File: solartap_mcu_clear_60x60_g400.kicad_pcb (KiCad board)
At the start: 2 copper layers, 70 x 70 mm, 24 parts, among them J1 USB_C_Receptacle_USB2.0_16P, U1 nRF52832-QFxx, U2 RS3002-3.3SYF5

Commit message: Продовая версия без fiducials
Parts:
- removed C13: 100n, Capacitor_SMD:C_0805_2012Metric_Pad1.18x1.45mm_HandSolder
- removed TP6: GND, TestPoint:TestPoint_Pad_D2.0mm
- added C7: 100p, Capacitor_SMD:C_0805_2012Metric, F.Cu at (86.5, 69.0)
- added C8: 100n, Capacitor_SMD:C_0805_2012Metric, F.Cu at (90.5, 57.0)
- added C9: TBD, Capacitor_SMD:C_0805_2012Metric, F.Cu at (86.0, 57.0)
- added TP4: GND, TestPoint:TestPoint_Pad_D2.0mm, F.Cu at (62.0, 64.5)
- added Y1: 32Mhz, Crystal:Crystal_SMD_3225-4Pin_3.2x2.5mm, F.Cu at (94.0, 69.5)
- BT1: value CR2032 -> CR927; footprint Battery:BatteryHolder_MPD_BC2003_1x2032 -> Battery:CR927
- C1: value 100n -> 16p; footprint Capacitor_SMD:C_0805_2012Metric_Pad1.18x1.45mm_HandSolder -> Capacitor_SMD:C_0805_2012Metric
- C10, C12: footprint Capacitor_SMD:C_0805_2012Metric_Pad1.18x1.45mm_HandSolder -> Capacitor_SMD:C_0805_2012Metric
- C11: value TBD -> 100n; footprint Capacitor_SMD:C_0805_2012Metric_Pad1.18x1.45mm_HandSolder -> Capacitor_SMD:C_0805_2012Metric
- C2: value 100p -> 16p; footprint Capacitor_SMD:C_0805_2012Metric_Pad1.18x1.45mm_HandSolder -> Capacitor_SMD:C_0805_2012Metric
- C3: value 1u -> 100n; footprint Capacitor_SMD:C_0805_2012Metric_Pad1.18x1.45mm_HandSolder -> Capacitor_SMD:C_0805_2012Metric
- C4: value 100n -> 4.7u; footprint Capacitor_SMD:C_0805_2012Metric_Pad1.18x1.45mm_HandSolder -> Capacitor_SMD:C_0805_2012Metric
- C5: value 4.7u -> 100n; footprint Capacitor_SMD:C_0805_2012Metric_Pad1.18x1.45mm_HandSolder -> Capacitor_SMD:C_0805_2012Metric
- C6: value 100n -> 1u; footprint Capacitor_SMD:C_0805_2012Metric_Pad1.18x1.45mm_HandSolder -> Capacitor_SMD:C_0805_2012Metric
- D1: moved to B.Cu
- D2: value RB751S-40 -> LBAT54CLT1G; footprint Diode_SMD:D_SOD-523 -> Package_TO_SOT_SMD:SOT-23-3
- J1: footprint Connector_USB:USB_C_Receptacle_GCT_USB4110 -> Connector_USB:USB_C_Receptacle_GCT_USB4105-xx-A_16P_TopMnt_Horizontal
- R1: value 100 -> 75; footprint Resistor_SMD:R_0805_2012Metric_Pad1.20x1.40mm_HandSolder -> Resistor_SMD:R_0805_2012Metric
- R2, R3: footprint Resistor_SMD:R_0805_2012Metric_Pad1.20x1.40mm_HandSolder -> Resistor_SMD:R_0805_2012Metric
- TP1: value RESET -> IO
- TP3: value IO -> RESET
- U2: footprint Package_TO_SOT_SMD:SOT-23-3 -> Package_TO_SOT_SMD:SOT-23-5
- moved TP5 72.7 mm to (62.0, 68.0)
- moved C11 56.6 mm to (112.5, 107.0), turned to -90 degrees
- moved R1 32.2 mm to (80.5, 75.0), turned to -90 degrees
- moved C5 14.2 mm to (80.0, 60.5)
- moved C4 13.7 mm to (94.0, 58.0)
- moved C1 12.5 mm to (90.5, 69.5), turned to 90 degrees
- moved C2 11.0 mm to (97.5, 69.5), turned to -90 degrees
- moved D1 11.0 mm to (70.0, 106.9)
- moved TP3 9.00 mm to (62.0, 71.5)
- moved TP1 7.00 mm to (62.0, 78.5)
- moved C3 3.20 mm to (91.5, 64.0), turned to 90 degrees
- moved C6 3.20 mm to (94.0, 62.0), turned to -90 degrees
- moved D2 3.16 mm to (115.5, 107.0), turned to 90 degrees
- moved TP2 1.00 mm to (62.0, 75.0)
- moved J1 0.50 mm to (95.0, 107.5)
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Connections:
- BT1 pad 1: +3.3V -> Net-(BT1-+)
- C1 pad 1: Net-(U1-DEC1) -> Net-(U1-XC1)
- C10 pad 1: GND -> Net-(U1-NFC1/P0.09)
- C10 pad 2: Net-(U1-NFC1/P0.09) -> GND
- C11 pad 1: Net-(U1-NFC1/P0.09) -> Net-(U2-OUT)
- C12 pad 1: Net-(U2-IN) -> Net-(U2-EN)
- C2 pad 1: Net-(U1-DEC3) -> Net-(U1-XC2)
- C3 pad 1: Net-(U1-DEC4) -> +3.3V
- C6 pad 1: +3.3V -> Net-(U1-DEC4)
- D1 pad 2: Net-(D1-A) -> +3.3V
- D2 pad 1: +3.3V -> Net-(U2-OUT)
- D2 pad 2: Net-(D2-A) -> Net-(BT1-+)
- J1 pad A4: Net-(U2-IN) -> Net-(U2-EN)
- J1 pad A9: Net-(U2-IN) -> Net-(U2-EN)
- J1 pad B4: Net-(U2-IN) -> Net-(U2-EN)
- J1 pad B9: Net-(U2-IN) -> Net-(U2-EN)
- R1 pad 1: Net-(D1-A) -> Net-(U1-P0.22)
- R1 pad 2: +3.3V -> Net-(D1-K)
- TP1 pad 1: Net-(U1-P0.21/~{RESET}) -> Net-(U1-SWDIO)
- TP3 pad 1: Net-(U1-SWDIO) -> Net-(U1-P0.21/~{RESET})
- U1 pad 27: Net-(D1-K) -> Net-(U1-P0.22)
- U1 pad 28: unconnected-(U1-P0.23-Pad28) -> Net-(D1-K)
- U1 pad 34: unconnected-(U1-XC1-Pad34) -> Net-(U1-XC1)
- U1 pad 35: unconnected-(U1-XC2-Pad35) -> Net-(U1-XC2)
- U2 pad 1: GND -> Net-(U2-EN)
- U2 pad 2: Net-(D2-A) -> GND
- U2 pad 3: Net-(U2-IN) -> Net-(U2-EN)
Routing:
- net Net-(BT1-+): track 0.00 -> 37.0 mm
- net GND: track 119.1 -> 154.5 mm, vias 9 -> 8
- net Net-(U2-EN): track 0.00 -> 23.1 mm
- net Net-(U2-IN): track 21.4 -> 0.00 mm
- net Net-(U1-XC2): track 0.00 -> 10.7 mm
- net Net-(U1-P0.22): track 0.00 -> 10.0 mm
- net Net-(U1-XC1): track 0.00 -> 8.14 mm
- net Net-(D2-A): track 5.95 -> 0.00 mm
- net unconnected-(U1-P0.24-Pad29): track 0.00 -> 5.84 mm
- net unconnected-(U1-P0.20-Pad23): track 0.00 -> 5.46 mm
- net Net-(U2-OUT): track 0.00 -> 5.42 mm
- net Net-(D1-K): track 41.8 -> 47.1 mm, vias 0 -> 1
- net unconnected-(U1-P0.19-Pad22): track 0.00 -> 5.21 mm
- net unconnected-(U1-P0.18/SWO-Pad21): track 0.00 -> 4.96 mm
- net unconnected-(U1-P0.17-Pad20): track 0.00 -> 4.72 mm
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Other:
- outline, holes or cut-outs redrawn
- board text added: "+"
- board text added: "+ БАТАРЕЙКИ ВВЕРХ"
- board text added: "20"
- board text added: "21"
- board text added: "22"
- board text added: "23"
- board text added: "29"
- board text added: "CR927 3V"
- board text added: "SolarTap/rev.D"
- board text removed: "G=400/C=15.249"

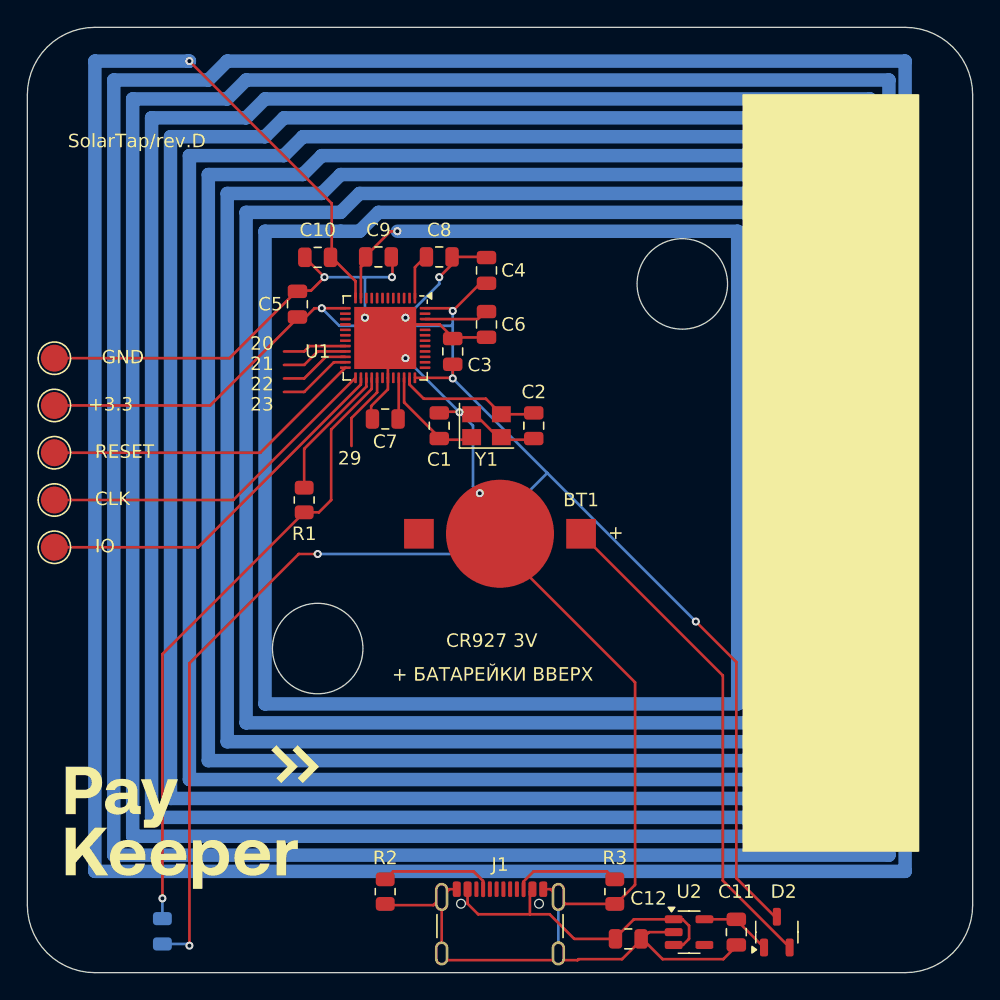
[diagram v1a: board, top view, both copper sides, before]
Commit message: Добавили fiducials
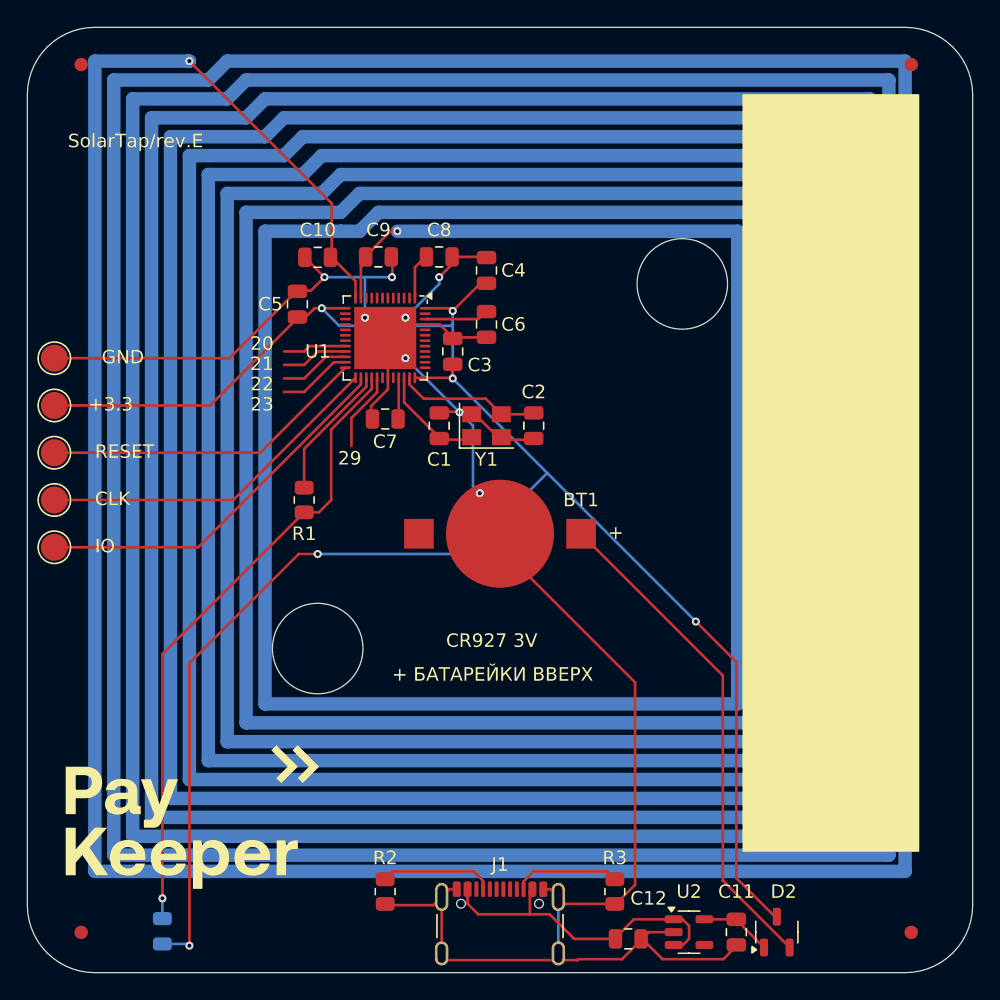
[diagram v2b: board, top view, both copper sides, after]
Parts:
- added REF**: Fiducial_1mm_Mask3mm, Fiducial:Fiducial_1mm_Mask3mm, F.Cu at (64.0, 107.0)
- added REF**: Fiducial_1mm_Mask3mm, Fiducial:Fiducial_1mm_Mask3mm, F.Cu at (125.5, 42.8)
- added REF**: Fiducial_1mm_Mask3mm, Fiducial:Fiducial_1mm_Mask3mm, F.Cu at (125.5, 107.0)
- added REF**: Fiducial_1mm_Mask3mm, Fiducial:Fiducial_1mm_Mask3mm, F.Cu at (64.0, 42.8)
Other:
- board text added: "SolarTap/rev.E"
- board text removed: "SolarTap/rev.D"

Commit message: Переделали схему под аккомулятор + добавили его чарджер. rev.F
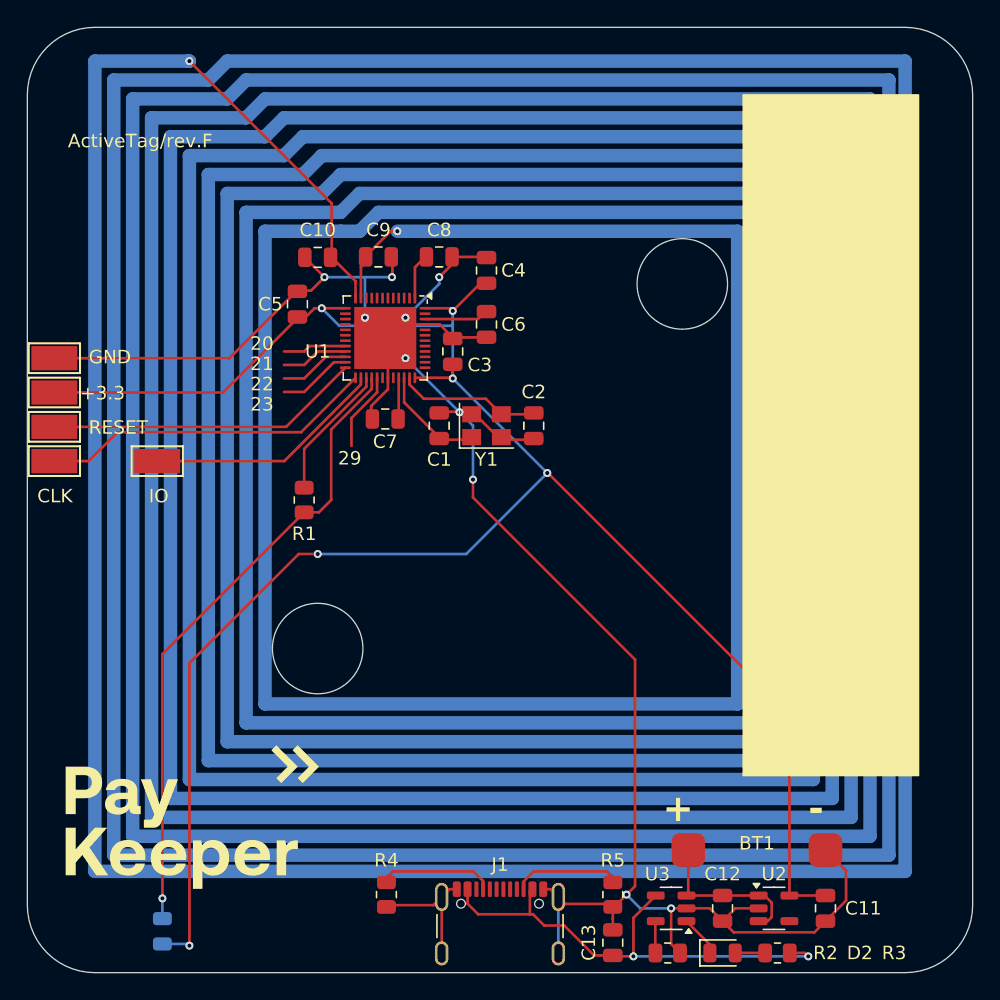
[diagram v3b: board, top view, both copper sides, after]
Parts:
- removed REF** (x4): Fiducial_1mm_Mask3mm, Fiducial:Fiducial_1mm_Mask3mm
- added C13: 100n, Capacitor_SMD:C_0805_2012Metric, F.Cu at (103.4, 107.8)
- added R4: 5.1k, Resistor_SMD:R_0805_2012Metric, F.Cu at (86.6, 104.2)
- added R5: 5.1k, Resistor_SMD:R_0805_2012Metric, F.Cu at (103.4, 104.2)
- added U3: LTC4054ES5-4.2, Package_TO_SOT_SMD:TSOT-23-5, F.Cu at (107.7, 105.2)
- BT1: value CR927 -> Li-Pol; footprint Battery:CR927 -> Battery:li-pol
- D2: value LBAT54CLT1G -> CHARGE; footprint Package_TO_SOT_SMD:SOT-23-3 -> LED_SMD:LED_0805_2012Metric
- R2: value 5.1k -> 10k
- TP1, TP2, TP3, TP4, TP5: footprint TestPoint:TestPoint_Pad_D2.0mm -> TestPoint:TestPoint_Keystone_5015_Micro-Minature
- moved BT1 30.2 mm to (114.0, 100.9)
- moved R2 21.4 mm to (107.4, 108.5), turned to 0 degrees
- moved R3 12.9 mm to (115.5, 108.5), turned to 180 degrees
- moved TP1 9.94 mm to (69.6, 72.1)
- moved C12 7.34 mm to (111.5, 105.2), turned to -90 degrees
- moved C11 6.83 mm to (119.1, 105.2)
- moved U2 6.53 mm to (115.3, 105.2)
- moved D2 4.30 mm to (111.5, 108.5), turned to 0 degrees
- moved TP2 2.88 mm to (62.0, 72.1)
- moved TP3 1.92 mm to (62.0, 69.6)
- moved TP5 0.96 mm to (62.0, 67.0)
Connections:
- C11 pad 1: Net-(U2-OUT) -> +3.3V
- C12 pad 1: Net-(U2-EN) -> Net-(BT1-+)
- D2 pad 1: Net-(U2-OUT) -> Net-(D2-K)
- D2 pad 2: Net-(BT1-+) -> Net-(D2-A)
- J1 pad A4: Net-(U2-EN) -> Net-(U3-V_{CC})
- J1 pad A9: Net-(U2-EN) -> Net-(U3-V_{CC})
- J1 pad B4: Net-(U2-EN) -> Net-(U3-V_{CC})
- J1 pad B9: Net-(U2-EN) -> Net-(U3-V_{CC})
- R2 pad 1: GND -> Net-(U3-PROG)
- R2 pad 2: Net-(J1-CC1) -> GND
- R3 pad 1: Net-(J1-CC2) -> Net-(U3-V_{CC})
- R3 pad 2: GND -> Net-(D2-A)
- U2 pad 1: Net-(U2-EN) -> Net-(BT1-+)
- U2 pad 3: Net-(U2-EN) -> Net-(BT1-+)
- U2 pad 5: Net-(U2-OUT) -> +3.3V
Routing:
- net Net-(U3-V_{CC}): track 0.00 -> 36.0 mm, vias 0 -> 2
- net Net-(BT1-+): track 37.0 -> 12.1 mm
- net Net-(U2-EN): track 23.1 -> 0.00 mm
- net Net-(U1-SWDIO): track 28.2 -> 17.9 mm
- net GND: track 154.5 -> 164.2 mm, vias 8 -> 10
- net Net-(U2-OUT): track 5.42 -> 0.00 mm
- net Net-(D2-K): track 0.00 -> 3.07 mm
- net Net-(U3-PROG): track 0.00 -> 2.36 mm
- net Net-(D2-A): track 0.00 -> 2.21 mm
- net +3.3V: track 153.8 -> 154.8 mm
- net Net-(U1-P0.21/~{RESET}): track 24.2 -> 23.4 mm
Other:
- board text added: "ActiveTag/rev.F"
- board text removed: "+"
- board text removed: "+ БАТАРЕЙКИ ВВЕРХ"
- board text removed: "CR927 3V"
- board text removed: "SolarTap/rev.E"

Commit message: Нет маски над контактами для прошивки, С3 подальше от микрухи, отверсия 4 мм в диаметре
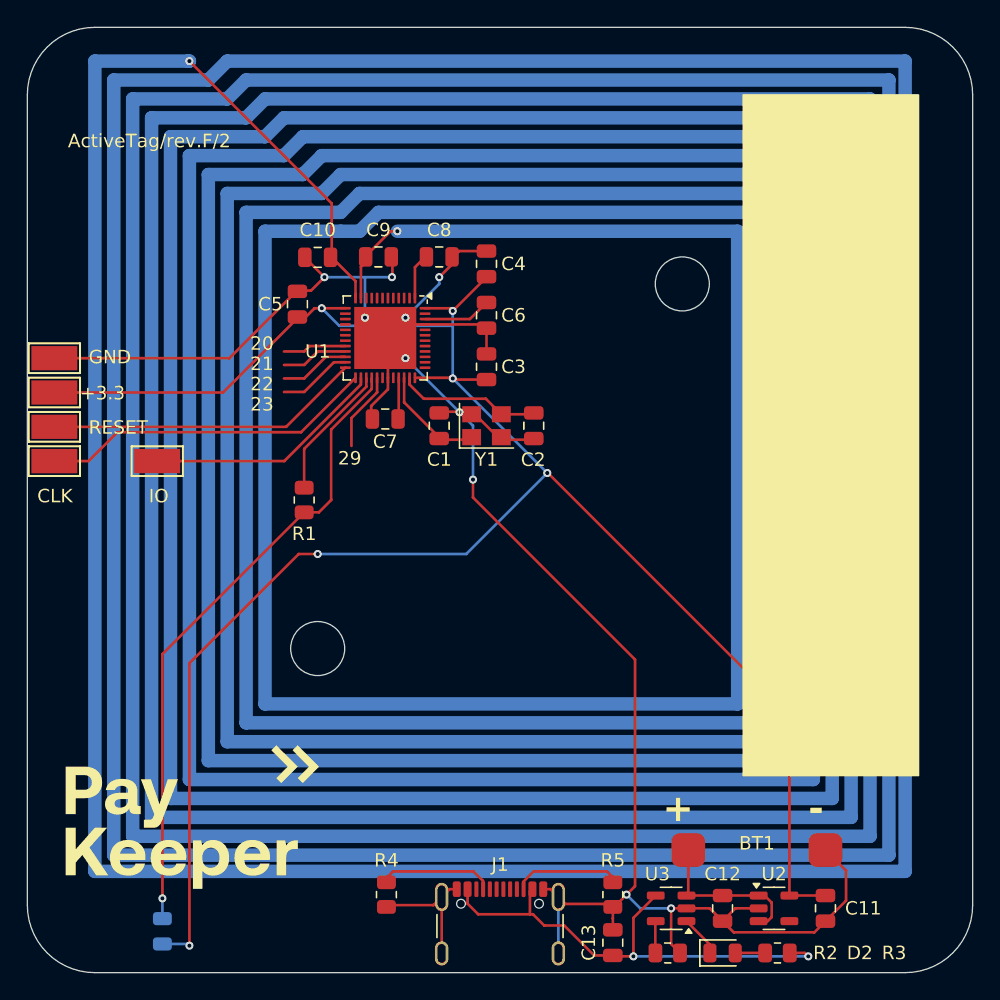
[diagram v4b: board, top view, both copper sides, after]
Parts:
- moved C3 2.75 mm to (94.0, 65.1)
- moved C6 0.67 mm to (94.0, 61.3)
- moved C4 0.48 mm to (94.0, 57.5)
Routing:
- net +3.3V: track 154.8 -> 156.7 mm
- net GND: track 164.2 -> 165.9 mm
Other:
- outline, holes or cut-outs redrawn
- board text added: "ActiveTag/rev.F/2"
- board text removed: "ActiveTag/rev.F"
